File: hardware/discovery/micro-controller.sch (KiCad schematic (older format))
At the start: 28 parts, among them U4 STM32F407VG, U8 MOLEX_microSD_47219-2001, X1 CRYSTAL

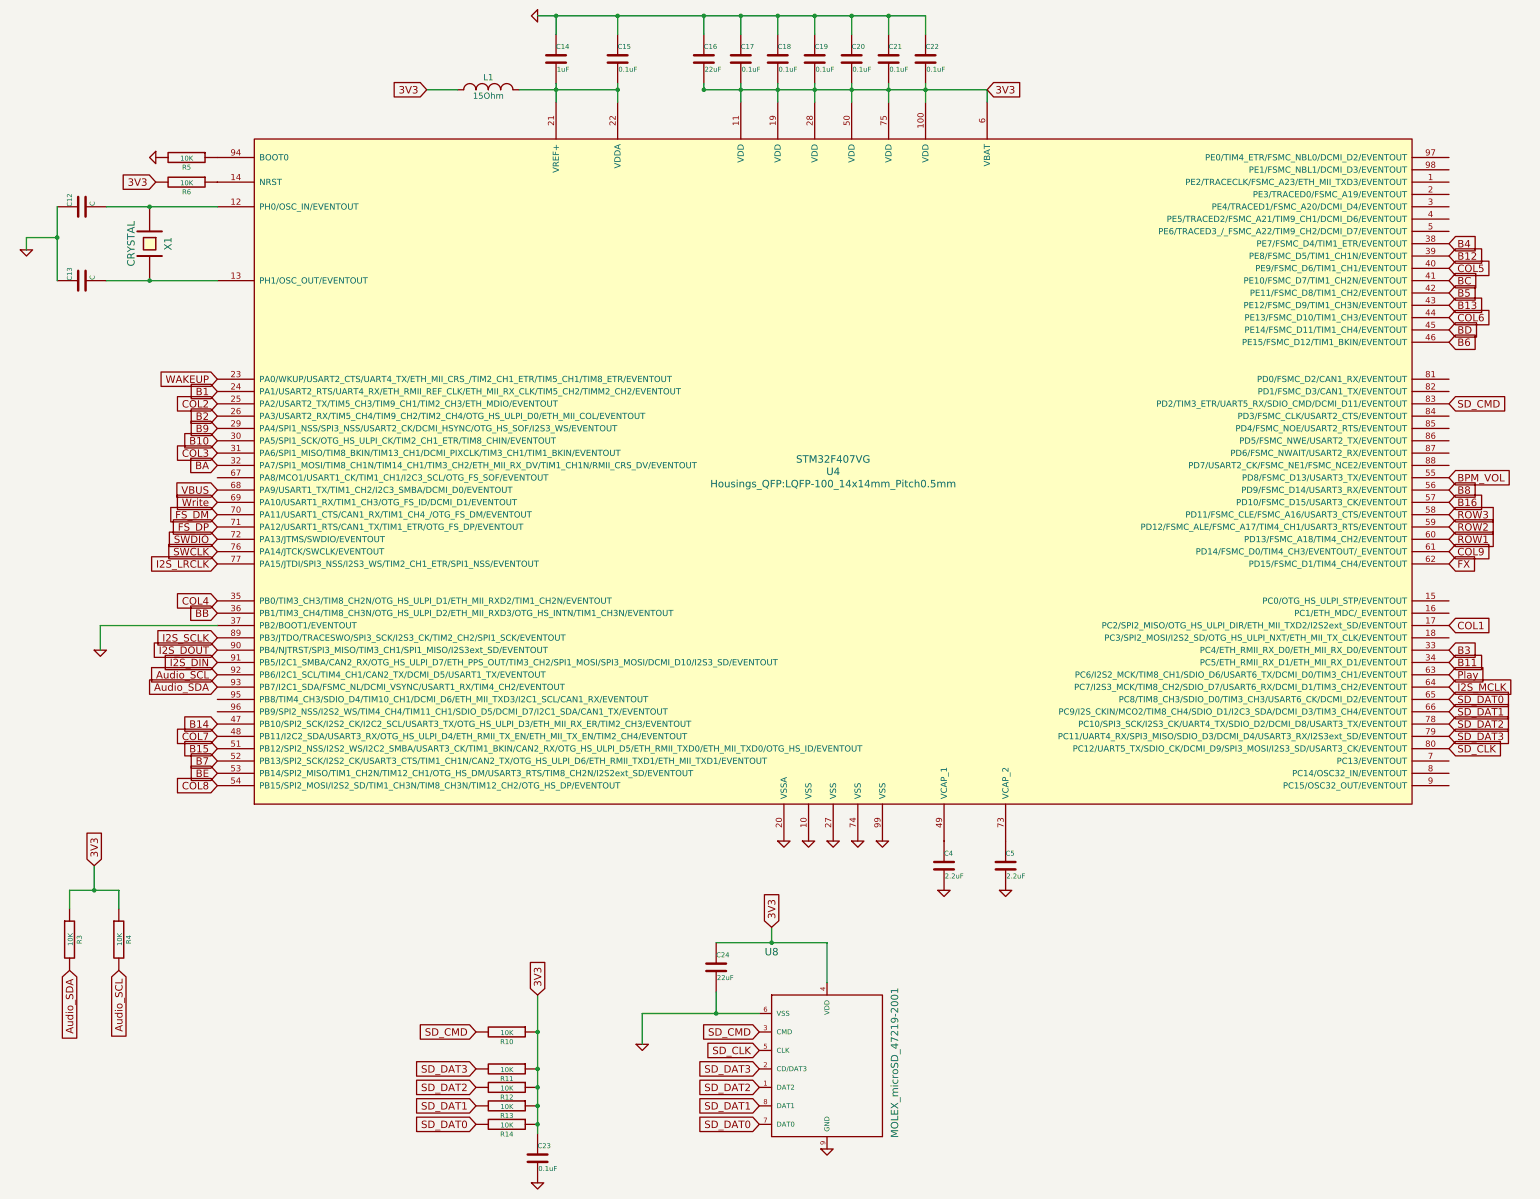
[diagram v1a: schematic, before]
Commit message: Discovery: Add two encoders and remove the BPM button
BPM and volume will be changed with a long press of the play button and
the encoders
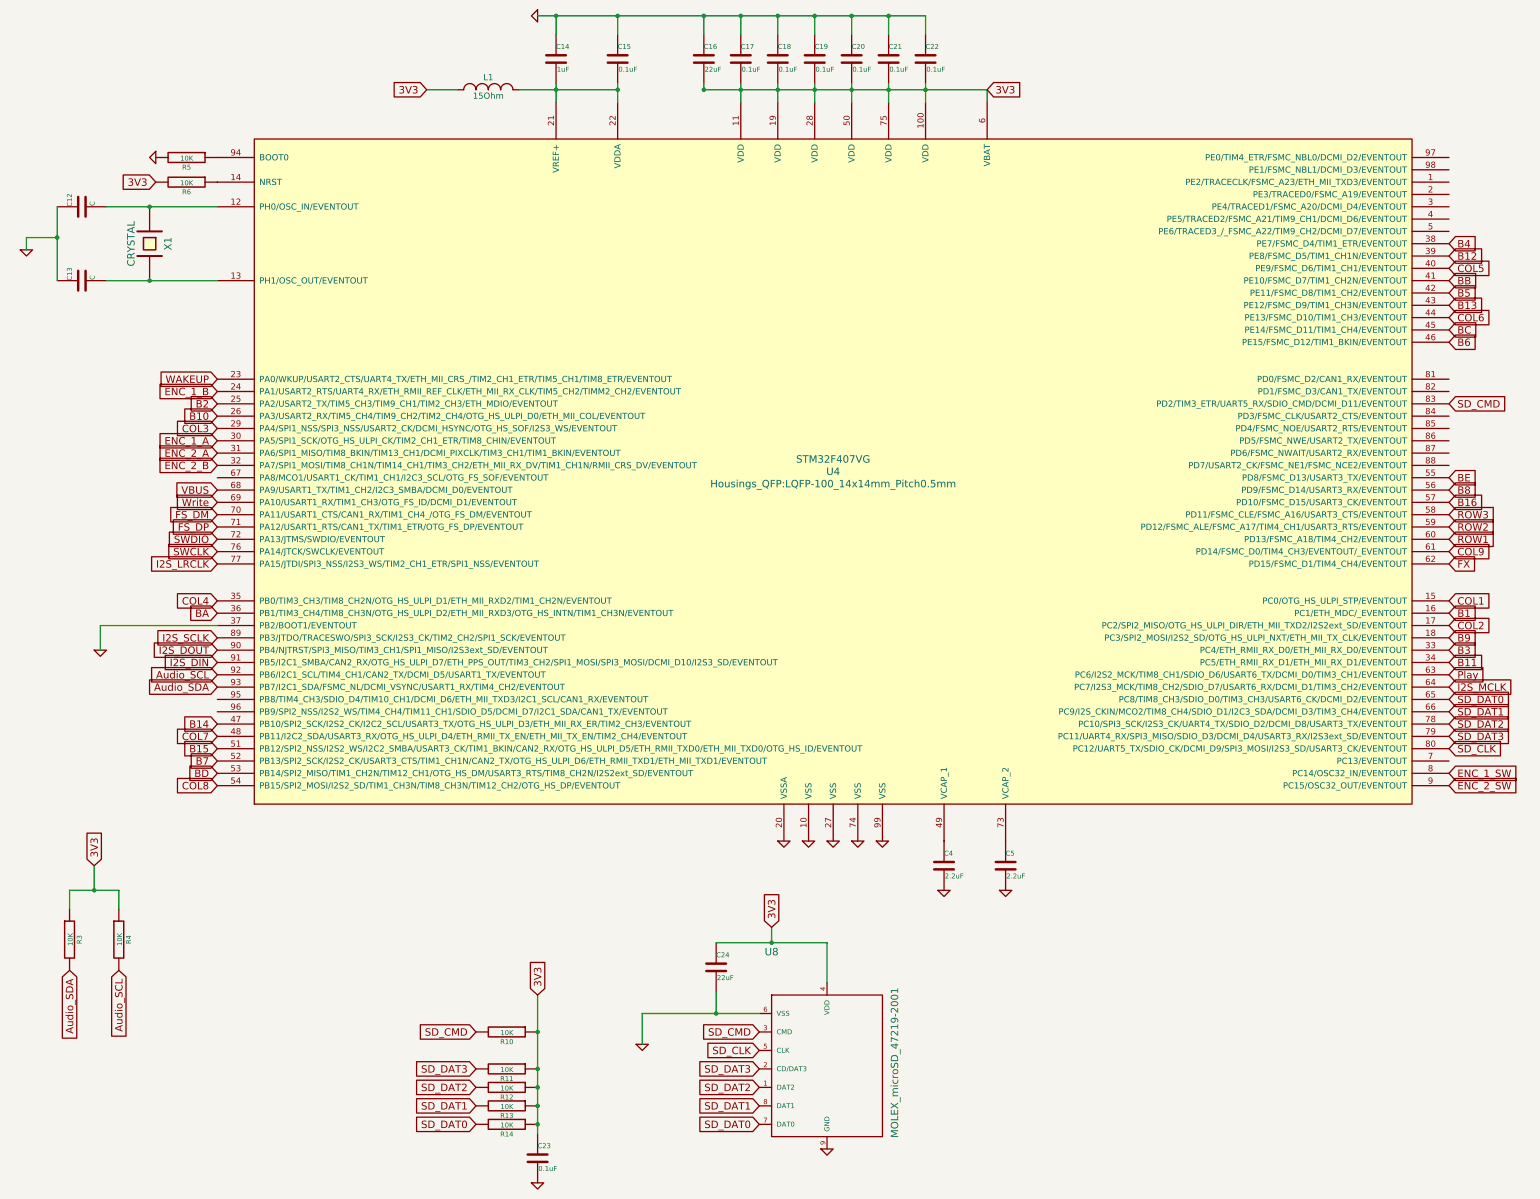
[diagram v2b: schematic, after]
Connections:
- net BPM_VOL is gone; now on net BE: U4.55 (PD8/FSMC_D13/USART3_TX/EVENTOUT)
- net B1: now also U4.16 (PC1/ETH_MDC/_EVENTOUT); no longer U4.24 (PA1/USART2_RTS/UART4_RX/ETH_RMII_REF_CLK/ETH_MII_RX_CLK/TIM5_CH2/TIMM2_CH2/EVENTOUT)
- net B10: now also U4.26 (PA3/USART2_RX/TIM5_CH4/TIM9_CH2/TIM2_CH4/OTG_HS_ULPI_D0/ETH_MII_COL/EVENTOUT); no longer U4.30 (PA5/SPI1_SCK/OTG_HS_ULPI_CK/TIM2_CH1_ETR/TIM8_CHIN/EVENTOUT)
- net B2: now also U4.25 (PA2/USART2_TX/TIM5_CH3/TIM9_CH1/TIM2_CH3/ETH_MDIO/EVENTOUT); no longer U4.26 (PA3/USART2_RX/TIM5_CH4/TIM9_CH2/TIM2_CH4/OTG_HS_ULPI_D0/ETH_MII_COL/EVENTOUT)
- net B9: now also U4.18 (PC3/SPI2_MOSI/I2S2_SD/OTG_HS_ULPI_NXT/ETH_MII_TX_CLK/EVENTOUT); no longer U4.29 (PA4/SPI1_NSS/SPI3_NSS/USART2_CK/DCMI_HSYNC/OTG_HS_SOF/I2S3_WS/EVENTOUT)
- net BA: now also U4.36 (PB1/TIM3_CH4/TIM8_CH3N/OTG_HS_ULPI_D2/ETH_MII_RXD3/OTG_HS_INTN/TIM1_CH3N/EVENTOUT); no longer U4.32 (PA7/SPI1_MOSI/TIM8_CH1N/TIM14_CH1/TIM3_CH2/ETH_MII_RX_DV/TIM1_CH1N/RMII_CRS_DV/EVENTOUT)
- net BB: now also U4.41 (PE10/FSMC_D7/TIM1_CH2N/EVENTOUT); no longer U4.36 (PB1/TIM3_CH4/TIM8_CH3N/OTG_HS_ULPI_D2/ETH_MII_RXD3/OTG_HS_INTN/TIM1_CH3N/EVENTOUT)
- net BC: now also U4.45 (PE14/FSMC_D11/TIM1_CH4/EVENTOUT); no longer U4.41 (PE10/FSMC_D7/TIM1_CH2N/EVENTOUT)
- net BD: now also U4.53 (PB14/SPI2_MISO/TIM1_CH2N/TIM12_CH1/OTG_HS_DM/USART3_RTS/TIM8_CH2N/I2S2ext_SD/EVENTOUT); no longer U4.45 (PE14/FSMC_D11/TIM1_CH4/EVENTOUT)
- net BE: no longer U4.53 (PB14/SPI2_MISO/TIM1_CH2N/TIM12_CH1/OTG_HS_DM/USART3_RTS/TIM8_CH2N/I2S2ext_SD/EVENTOUT)
- net COL1: now also U4.15 (PC0/OTG_HS_ULPI_STP/EVENTOUT); no longer U4.17 (PC2/SPI2_MISO/OTG_HS_ULPI_DIR/ETH_MII_TXD2/I2S2ext_SD/EVENTOUT)
- net COL2: now also U4.17 (PC2/SPI2_MISO/OTG_HS_ULPI_DIR/ETH_MII_TXD2/I2S2ext_SD/EVENTOUT); no longer U4.25 (PA2/USART2_TX/TIM5_CH3/TIM9_CH1/TIM2_CH3/ETH_MDIO/EVENTOUT)
- net COL3: now also U4.29 (PA4/SPI1_NSS/SPI3_NSS/USART2_CK/DCMI_HSYNC/OTG_HS_SOF/I2S3_WS/EVENTOUT); no longer U4.31 (PA6/SPI1_MISO/TIM8_BKIN/TIM13_CH1/DCMI_PIXCLK/TIM3_CH1/TIM1_BKIN/EVENTOUT)
- net ENC_1_SW: now reaches U4.8 (PC14/OSC32_IN/EVENTOUT)
- net ENC_2_SW: now reaches U4.9 (PC15/OSC32_OUT/EVENTOUT)
- new net ENC_1_A: U4.30 (PA5/SPI1_SCK/OTG_HS_ULPI_CK/TIM2_CH1_ETR/TIM8_CHIN/EVENTOUT)
- new net ENC_1_B: U4.24 (PA1/USART2_RTS/UART4_RX/ETH_RMII_REF_CLK/ETH_MII_RX_CLK/TIM5_CH2/TIMM2_CH2/EVENTOUT)
- new net ENC_2_A: U4.31 (PA6/SPI1_MISO/TIM8_BKIN/TIM13_CH1/DCMI_PIXCLK/TIM3_CH1/TIM1_BKIN/EVENTOUT)
- new net ENC_2_B: U4.32 (PA7/SPI1_MOSI/TIM8_CH1N/TIM14_CH1/TIM3_CH2/ETH_MII_RX_DV/TIM1_CH1N/RMII_CRS_DV/EVENTOUT)
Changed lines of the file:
@@
 FS_DP
 $Comp
-L GND #PWR011
+L GND #PWR013
 U 1 1 585E3358
 P 7650 7850
-F 0 "#PWR011" H 7650 7850 30  0001 C CNN
+F 0 "#PWR013" H 7650 7850 30  0001 C CNN
 F 1 "GND" H 7650 7780 30  0001 C CNN
 F 2 "" H 7650 7850 60  0001 C CNN
@@
 $EndComp
 $Comp
-L GND #PWR012
+L GND #PWR014
 U 1 1 585E336D
 P 7850 7850
-F 0 "#PWR012" H 7850 7850 30  0001 C CNN
+F 0 "#PWR014" H 7850 7850 30  0001 C CNN
 F 1 "GND" H 7850 7780 30  0001 C CNN
 F 2 "" H 7850 7850 60  0001 C CNN
@@
 $EndComp
 $Comp
-L GND #PWR013
+L GND #PWR015
 U 1 1 585E337B
 P 8050 7850
-F 0 "#PWR013" H 8050 7850 30  0001 C CNN
+F 0 "#PWR015" H 8050 7850 30  0001 C CNN
 F 1 "GND" H 8050 7780 30  0001 C CNN
 F 2 "" H 8050 7850 60  0001 C CNN
@@
 $EndComp
 $Comp
-L GND #PWR014
+L GND #PWR016
 U 1 1 585E3389
 P 8250 7850
-F 0 "#PWR014" H 8250 7850 30  0001 C CNN
+F 0 "#PWR016" H 8250 7850 30  0001 C CNN
 F 1 "GND" H 8250 7780 30  0001 C CNN
 F 2 "" H 8250 7850 60  0001 C CNN
@@
 $EndComp
 $Comp
-L GND #PWR015
+L GND #PWR017
 U 1 1 585E3397
 P 7450 7850
-F 0 "#PWR015" H 7450 7850 30  0001 C CNN
+F 0 "#PWR017" H 7450 7850 30  0001 C CNN
 F 1 "GND" H 7450 7780 30  0001 C CNN
 F 2 "" H 7450 7850 60  0001 C CNN
@@
 $EndComp
 $Comp
-L GND #PWR016
+L GND #PWR018
 U 1 1 585E35DF
 P 8750 8250
-F 0 "#PWR016" H 8750 8250 30  0001 C CNN
+F 0 "#PWR018" H 8750 8250 30  0001 C CNN
 F 1 "GND" H 8750 8180 30  0001 C CNN
 F 2 "" H 8750 8250 60  0001 C CNN
@@
 $EndComp
 $Comp
-L GND #PWR017
+L GND #PWR019
 U 1 1 585E35F3
 P 9250 8250
-F 0 "#PWR017" H 9250 8250 30  0001 C CNN
+F 0 "#PWR019" H 9250 8250 30  0001 C CNN
 F 1 "GND" H 9250 8180 30  0001 C CNN
 F 2 "" H 9250 8250 60  0001 C CNN
@@
 $EndComp
 $Comp
-L GND #PWR018
+L GND #PWR020
 U 1 1 585F8908
 P 1300 3050
-F 0 "#PWR018" H 1300 3050 30  0001 C CNN
+F 0 "#PWR020" H 1300 3050 30  0001 C CNN
 F 1 "GND" H 1300 2980 30  0001 C CNN
 F 2 "" H 1300 3050 60  0001 C CNN
@@
 $EndComp
 $Comp
-L GND #PWR019
+L GND #PWR021
 U 1 1 58612418
 P 2350 2300
-F 0 "#PWR019" H 2350 2300 30  0001 C CNN
+F 0 "#PWR021" H 2350 2300 30  0001 C CNN
 F 1 "GND" H 2350 2230 30  0001 C CNN
 F 2 "" H 2350 2300 60  0001 C CNN
@@
 3V3
 $Comp
-L GND #PWR020
+L GND #PWR022
 U 1 1 58612E50
 P 5450 1150
-F 0 "#PWR020" H 5450 1150 30  0001 C CNN
+F 0 "#PWR022" H 5450 1150 30  0001 C CNN
 F 1 "GND" H 5450 1080 30  0001 C CNN
 F 2 "" H 5450 1150 60  0001 C CNN
@@
 $EndComp
 $Comp
-L GND #PWR021
+L GND #PWR023
 U 1 1 5861353A
 P 1900 6300
-F 0 "#PWR021" H 1900 6300 30  0001 C CNN
+F 0 "#PWR023" H 1900 6300 30  0001 C CNN
 F 1 "GND" H 1900 6230 30  0001 C CNN
 F 2 "" H 1900 6300 60  0001 C CNN
@@
 B8
 Text GLabel 12850 4900 2    60   Input ~ 0
-BPM_VOL
+BE
 Text GLabel 2850 7400 0    60   Input ~ 0
 COL8
@@
 B7
 Text GLabel 2850 7300 0    60   Input ~ 0
-BE
+BD
 Text GLabel 2850 7000 0    60   Input ~ 0
 COL7
@@
 B6
 Text GLabel 12850 3700 2    60   Input ~ 0
-BD
+BC
 Text GLabel 12850 3600 2    60   Input ~ 0
 COL6
@@
 B5
 Text GLabel 12850 3300 2    60   Input ~ 0
-BC
+BB
 Text GLabel 12850 3200 2    60   Input ~ 0
 COL5
@@
 $EndComp
 $Comp
-L GND #PWR022
+L GND #PWR024
 U 1 1 586394FE
 P 7800 10350
-F 0 "#PWR022" H 7800 10350 30  0001 C CNN
+F 0 "#PWR024" H 7800 10350 30  0001 C CNN
 F 1 "GND" H 7800 10280 30  0001 C CNN
 F 2 "" H 7800 10350 60  0001 C CNN
@@
 SD_CMD
 $Comp
-L GND #PWR023
+L GND #PWR025
 U 1 1 58631320
 P 6300 9500
-F 0 "#PWR023" H 6300 9500 30  0001 C CNN
+F 0 "#PWR025" H 6300 9500 30  0001 C CNN
 F 1 "GND" H 6300 9430 30  0001 C CNN
 F 2 "" H 6300 9500 60  0001 C CNN
@@
 B4
 Text GLabel 2850 6000 0    60   Input ~ 0
-BB
+BA
 Text GLabel 2850 5900 0    60   Input ~ 0
 COL4
@@
 Text GLabel 12850 6300 2    60   Input ~ 0
 B3
-Text GLabel 2850 4800 0    60   Input ~ 0
-BA
-Text GLabel 2850 4700 0    60   Input ~ 0
+Text GLabel 2850 4500 0    60   Input ~ 0
 COL3
-Text GLabel 2850 4600 0    60   Input ~ 0
+Text GLabel 2850 4400 0    60   Input ~ 0
 B10
-Text GLabel 2850 4500 0    60   Input ~ 0
+Text GLabel 12850 6200 2    60   Input ~ 0
 B9
-Text GLabel 2850 4400 0    60   Input ~ 0
+Text GLabel 2850 4300 0    60   Input ~ 0
 B2
-Text GLabel 2850 4300 0    60   Input ~ 0
+Text GLabel 12850 6100 2    60   Input ~ 0
 COL2
-Text GLabel 2850 4200 0    60   Input ~ 0
+Text GLabel 12850 6000 2    60   Input ~ 0
 B1
-Text GLabel 12850 6100 2    60   Input ~ 0
+Text GLabel 12850 5900 2    60   Input ~ 0
 COL1
 $Comp
@@
 $EndComp
 $Comp
-L GND #PWR024
+L GND #PWR026
 U 1 1 58640311
 P 5450 10625
-F 0 "#PWR024" H 5450 10625 30  0001 C CNN
+F 0 "#PWR026" H 5450 10625 30  0001 C CNN
 F 1 "GND" H 5450 10555 30  0001 C CNN
 F 2 "" H 5450 10625 60  0001 C CNN
@@
 	7350 8550 7350 8675
 Connection ~ 7350 8675
+Text GLabel 2850 4600 0    60   Input ~ 0
+ENC_1_A
+Text GLabel 2850 4200 0    60   Input ~ 0
+ENC_1_B
+Text GLabel 2850 4700 0    60   Input ~ 0
+ENC_2_A
+Text GLabel 2850 4800 0    60   Input ~ 0
+ENC_2_B
+Text GLabel 12850 7300 2    60   Input ~ 0
+ENC_1_SW
+Text GLabel 12850 7400 2    60   Input ~ 0
+ENC_2_SW
 $EndSCHEMATC
